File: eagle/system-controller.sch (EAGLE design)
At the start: 226 parts, among them J1 1, Q1 MOSFET-P-N-PAIR, Q10 MOSFET-P-N-PAIR, Q11 DNP/NTR4101P, Q2 MOSFET-P-N-PAIR, Q3 DON3035L, Q4 MOSFET-P-N-PAIR, Q5 MOSFET-P-N-PAIR, Q6 MOSFET-P-N-PAIR, Q7 MOSFET-P-N-PAIR, Q8 MOSFET-P-N-PAIR, Q9 DNP/NTR4101P, U1 TPS25944LRVCRWQFN-20-3X4, U10 TPS25944LRVCRWQFN-20-3X4, U11 ACPL-M61L, U12 ACPL-M61L, U13 TPS25944LRVCRWQFN-20-3X4, U14 ACPL-M61L, U15 ACPL-M61L, U2 LP5907MFX-3.0, U3 TPS25944LRVCRWQFN-20-3X4, U4 TPS25944LRVCRWQFN-20-3X4, U5 TPS25944LRVCRWQFN-20-3X4, U6 TPS25944LRVCRWQFN-20-3X4, U7 ATMEGA128L-8A(U/N), U8 TS4100, U9 TPS25944LRVCRWQFN-20-3X4, X1 8 MHz CRYSTAL-ABRACON-ABM3-SMD

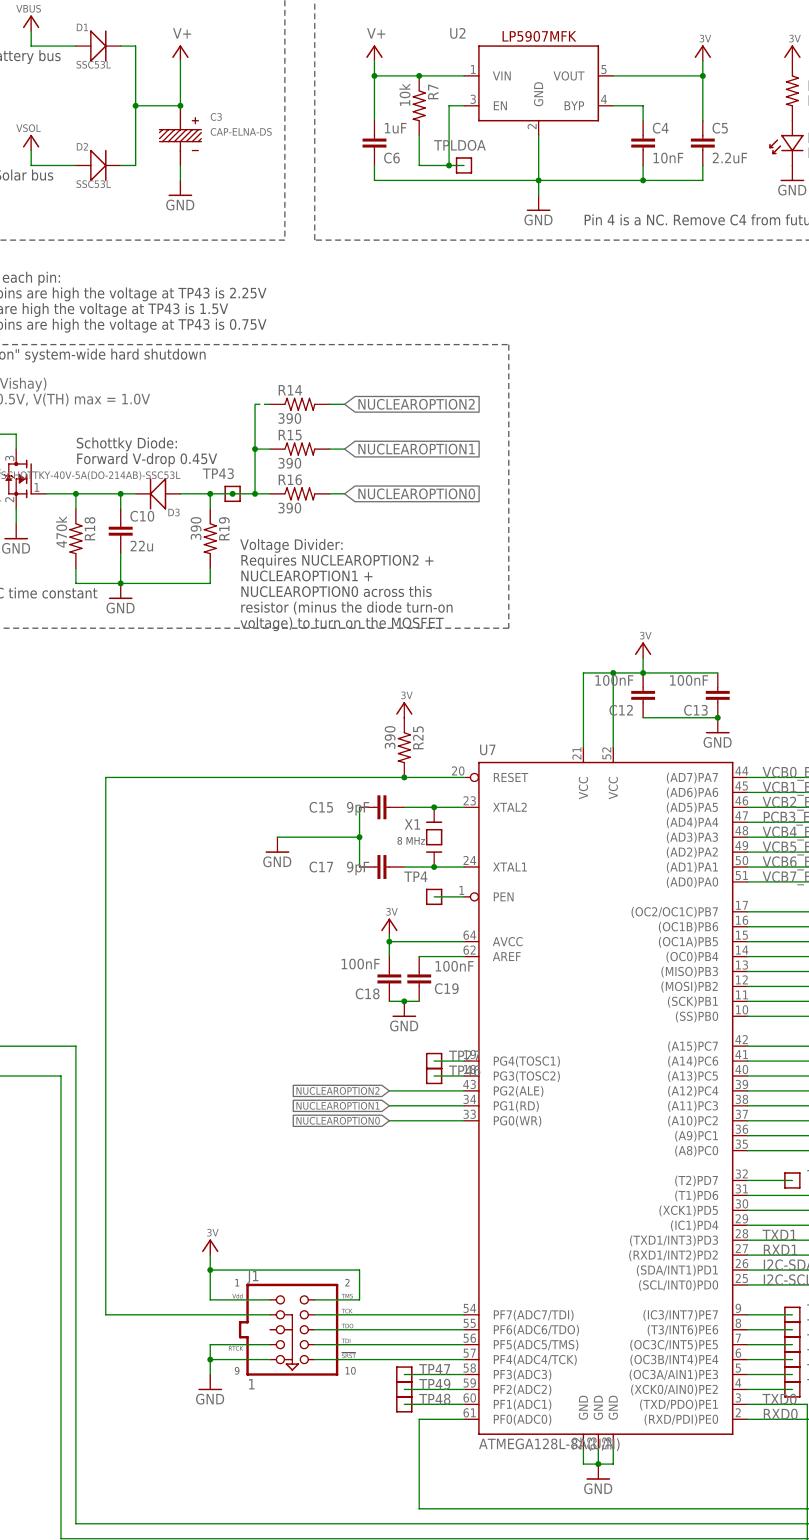
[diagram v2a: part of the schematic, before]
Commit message: Fixed some of the remaining issues such as JTAG layout and schematic, 0 ohm resistors, etc. Check the issue section on the git for more info
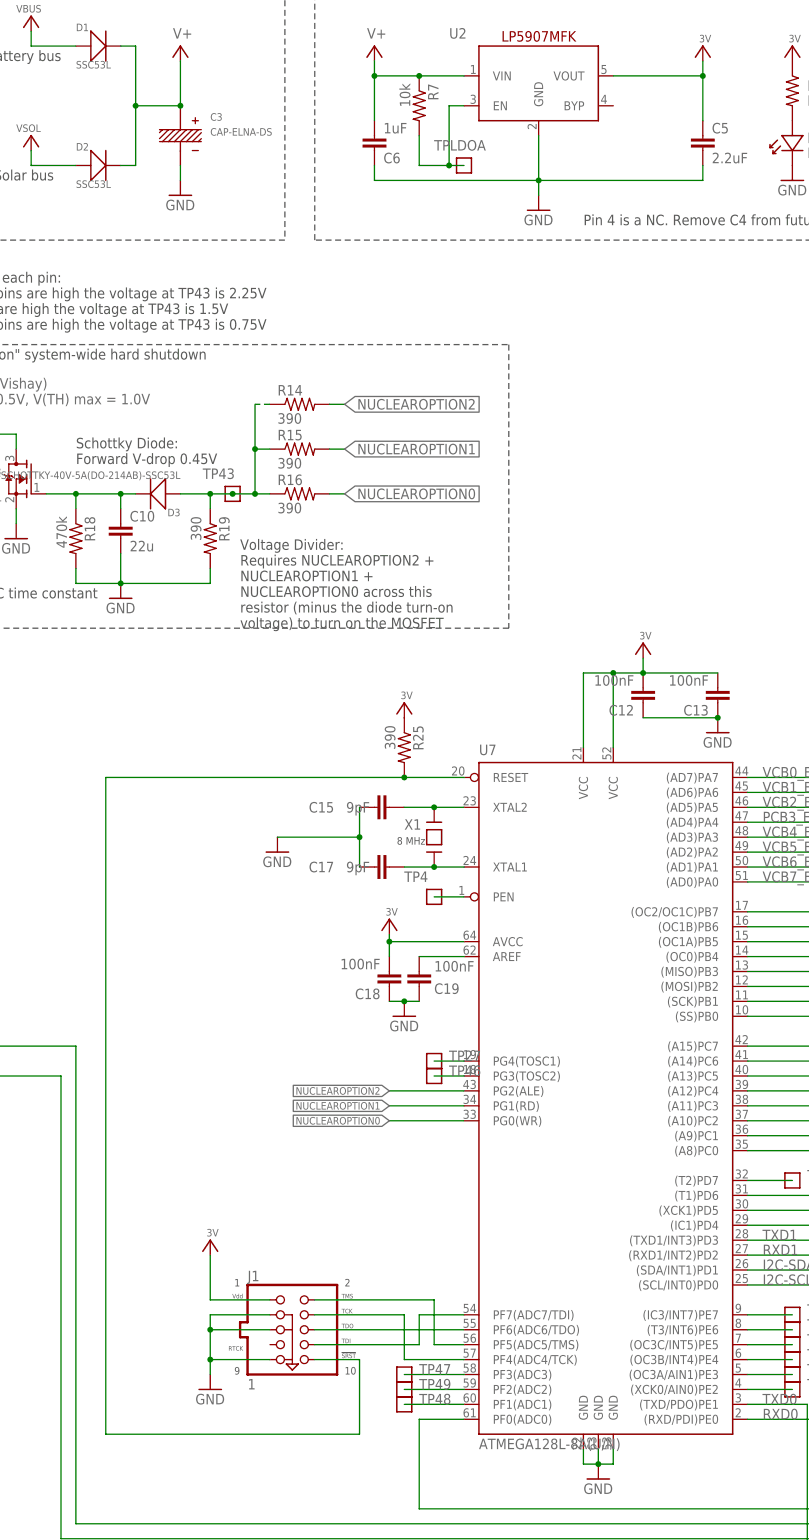
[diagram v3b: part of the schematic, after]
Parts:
- removed C4: 10nF, rcl_custom:C-EU0603-B-NOSILK
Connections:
- removed net N$23: C4.1, U2.BYP
- net 3V: no longer J1.TMS
- net GND: now also J1.GND3, J1.GND5; no longer C4.2, J1.RTCK
- net N$11: now also J1.TCK; no longer J1.SRST
- net N$13: now also U7.PF7(ADC7/TDI); no longer U7.PF5(ADC5/TMS)
- net N$14: now also J1.TMS, U7.PF5(ADC5/TMS); no longer J1.TCK, U7.PF7(ADC7/TDI)
- net N$15: now also J1.SRST; no longer J1.GND3
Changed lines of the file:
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@@
 <?xml version="1.0" encoding="utf-8"?>
 <!DOCTYPE eagle SYSTEM "eagle.dtd">
-<eagle version="7.5.0">
+<eagle version="7.6.0">
 <drawing>
 <settings>
@@
 <attribute name="MPN" value="CL10A225KQ8NNNC"/>
 </part>
-<part name="C4" library="rcl_custom" deviceset="C-EU" device="0603-B-NOSILK" value="10nF">
-<attribute name="DIST" value="digikey"/>
-<attribute name="DPN" value="399-1092-1-ND"/>
-<attribute name="MFN" value="Kemet"/>
-<attribute name="MPN" value="C0603C103J5RACTU"/>
-</part>
 <part name="SUPPLY9" library="psas_c3_team05" deviceset="V+" device=""/>
 <part name="X1" library="crystal-abracon-abm3-smd" deviceset="CRYSTAL-ABRACON-ABM3-SMD" device="" value="8 MHz CRYSTAL-ABRACON-ABM3-SMD">
@@
 <attribute name="MPN" x="195.58" y="378.46" size="1.778" layer="96" display="off"/>
 </instance>
-<instance part="C4" gate="CE" x="185.42" y="378.46">
-<attribute name="DIST" x="185.42" y="378.46" size="1.778" layer="96" display="off"/>
-<attribute name="DPN" x="185.42" y="378.46" size="1.778" layer="96" display="off"/>
-<attribute name="MFN" x="185.42" y="378.46" size="1.778" layer="96" display="off"/>
-<attribute name="MPN" x="185.42" y="378.46" size="1.778" layer="96" display="off"/>
-</instance>
 <instance part="SUPPLY9" gate="1" x="106.68" y="393.7"/>
 <instance part="X1" gate="G$1" x="149.86" y="259.08" smashed="yes" rot="R270">
@@
 </segment>
 </net>
-<net name="N$11" class="0">
-<segment>
-<pinref part="U7" gate="G$1" pin="PF4(ADC4/TCK)"/>
-<wire x1="129.54" y1="170.18" x2="154.94" y2="170.18" width="0.1524" layer="91"/>
-<pinref part="J1" gate="J" pin="SRST"/>
-</segment>
-</net>
-<net name="N$12" class="0">
-<segment>
-<pinref part="U7" gate="G$1" pin="PF6(ADC6/TDO)"/>
-<wire x1="129.54" y1="175.26" x2="154.94" y2="175.26" width="0.1524" layer="91"/>
-<pinref part="J1" gate="J" pin="TDO"/>
-</segment>
-</net>
-<net name="N$13" class="0">
-<segment>
-<pinref part="U7" gate="G$1" pin="PF5(ADC5/TMS)"/>
-<wire x1="129.54" y1="172.72" x2="154.94" y2="172.72" width="0.1524" layer="91"/>
-<pinref part="J1" gate="J" pin="TDI"/>
-</segment>
-</net>
-<net name="N$14" class="0">
-<segment>
-<pinref part="U7" gate="G$1" pin="PF7(ADC7/TDI)"/>
-<wire x1="129.54" y1="177.8" x2="154.94" y2="177.8" width="0.1524" layer="91"/>
-<pinref part="J1" gate="J" pin="TCK"/>
-</segment>
-</net>
 <net name="N$15" class="0">
 <segment>
@@
 <wire x1="154.94" y1="269.24" x2="144.78" y2="269.24" width="0.1524" layer="91"/>
 <wire x1="144.78" y1="269.24" x2="93.98" y2="269.24" width="0.1524" layer="91"/>
-<wire x1="93.98" y1="269.24" x2="93.98" y2="177.8" width="0.1524" layer="91"/>
-<wire x1="93.98" y1="177.8" x2="121.92" y2="177.8" width="0.1524" layer="91"/>
+<wire x1="93.98" y1="269.24" x2="93.98" y2="157.48" width="0.1524" layer="91"/>
 <pinref part="R25" gate="R" pin="2"/>
 <junction x="144.78" y="269.24"/>
-<pinref part="J1" gate="J" pin="GND3"/>
+<wire x1="93.98" y1="157.48" x2="137.16" y2="157.48" width="0.1524" layer="91"/>
+<wire x1="137.16" y1="157.48" x2="137.16" y2="170.18" width="0.1524" layer="91"/>
+<pinref part="J1" gate="J" pin="SRST"/>
+<wire x1="137.16" y1="170.18" x2="129.54" y2="170.18" width="0.1524" layer="91"/>
 </segment>
 </net>
@@
 </segment>
 </net>
-<net name="N$23" class="0">
-<segment>
-<pinref part="C4" gate="CE" pin="1"/>
-<wire x1="180.34" y1="383.54" x2="185.42" y2="383.54" width="0.1524" layer="91"/>
-<wire x1="185.42" y1="383.54" x2="185.42" y2="381" width="0.1524" layer="91"/>
-<pinref part="U2" gate="G$1" pin="BYP"/>
-</segment>
-</net>
 <net name="N$1" class="0">
 <segment>
@@
 </segment>
 <segment>
-<wire x1="137.16" y1="185.42" x2="137.16" y2="180.34" width="0.1524" layer="91"/>
-<wire x1="111.76" y1="185.42" x2="137.16" y2="185.42" width="0.1524" layer="91"/>
 <wire x1="121.92" y1="180.34" x2="111.76" y2="180.34" width="0.1524" layer="91"/>
-<wire x1="111.76" y1="180.34" x2="111.76" y2="185.42" width="0.1524" layer="91"/>
+<wire x1="111.76" y1="180.34" x2="111.76" y2="187.96" width="0.1524" layer="91"/>
 <pinref part="3V-3" gate="G$1" pin="3V"/>
-<wire x1="111.76" y1="187.96" x2="111.76" y2="185.42" width="0.1524" layer="91"/>
-<junction x="111.76" y="185.42"/>
 <pinref part="J1" gate="J" pin="VDD"/>
-<pinref part="J1" gate="J" pin="TMS"/>
-<wire x1="129.54" y1="180.34" x2="137.16" y2="180.34" width="0.1524" layer="91"/>
 </segment>
 <segment>
@@
 <pinref part="C5" gate="CE" pin="2"/>
 <wire x1="195.58" y1="370.84" x2="195.58" y2="373.38" width="0.1524" layer="91"/>
-<wire x1="167.64" y1="370.84" x2="185.42" y2="370.84" width="0.1524" layer="91"/>
-<pinref part="C4" gate="CE" pin="2"/>
-<wire x1="185.42" y1="370.84" x2="195.58" y2="370.84" width="0.1524" layer="91"/>
-<wire x1="185.42" y1="373.38" x2="185.42" y2="370.84" width="0.1524" layer="91"/>
-<junction x="185.42" y="370.84"/>
+<wire x1="167.64" y1="370.84" x2="195.58" y2="370.84" width="0.1524" layer="91"/>
 <pinref part="C6" gate="CE" pin="1"/>
 <pinref part="U2" gate="G$1" pin="GND"/>
@@
 <segment>
 <pinref part="GND3" gate="1" pin="GND"/>
-<wire x1="121.92" y1="172.72" x2="111.76" y2="172.72" width="0.1524" layer="91"/>
-<wire x1="111.76" y1="172.72" x2="111.76" y2="170.18" width="0.1524" layer="91"/>
 <wire x1="121.92" y1="170.18" x2="111.76" y2="170.18" width="0.1524" layer="91"/>
 <junction x="111.76" y="170.18"/>
 <wire x1="111.76" y1="170.18" x2="111.76" y2="167.64" width="0.1524" layer="91"/>
 <pinref part="J1" gate="J" pin="GND9"/>
-<pinref part="J1" gate="J" pin="RTCK"/>
+<pinref part="J1" gate="J" pin="GND5"/>
+<wire x1="121.92" y1="175.26" x2="111.76" y2="175.26" width="0.1524" layer="91"/>
+<wire x1="111.76" y1="175.26" x2="111.76" y2="170.18" width="0.1524" layer="91"/>
+<pinref part="J1" gate="J" pin="GND3"/>
+<wire x1="121.92" y1="177.8" x2="111.76" y2="177.8" width="0.1524" layer="91"/>
+<wire x1="111.76" y1="177.8" x2="111.76" y2="175.26" width="0.1524" layer="91"/>
+<junction x="111.76" y="175.26"/>
 </segment>
 <segment>
@@
 </segment>
 </net>
+<net name="N$11" class="0">
+<segment>
+<pinref part="J1" gate="J" pin="TCK"/>
+<wire x1="129.54" y1="177.8" x2="144.78" y2="177.8" width="0.1524" layer="91"/>
+<wire x1="144.78" y1="177.8" x2="144.78" y2="170.18" width="0.1524" layer="91"/>
+<pinref part="U7" gate="G$1" pin="PF4(ADC4/TCK)"/>
+<wire x1="144.78" y1="170.18" x2="154.94" y2="170.18" width="0.1524" layer="91"/>
+</segment>
+</net>
+<net name="N$12" class="0">
+<segment>
+<pinref part="J1" gate="J" pin="TDO"/>
+<pinref part="U7" gate="G$1" pin="PF6(ADC6/TDO)"/>
+<wire x1="129.54" y1="175.26" x2="154.94" y2="175.26" width="0.1524" layer="91"/>
+</segment>
+</net>
+<net name="N$13" class="0">
+<segment>
+<pinref part="J1" gate="J" pin="TDI"/>
+<wire x1="129.54" y1="172.72" x2="147.32" y2="172.72" width="0.1524" layer="91"/>
+<wire x1="147.32" y1="172.72" x2="147.32" y2="177.8" width="0.1524" layer="91"/>
+<pinref part="U7" gate="G$1" pin="PF7(ADC7/TDI)"/>
+<wire x1="147.32" y1="177.8" x2="154.94" y2="177.8" width="0.1524" layer="91"/>
+</segment>
+</net>
+<net name="N$14" class="0">
+<segment>
+<pinref part="J1" gate="J" pin="TMS"/>
+<wire x1="129.54" y1="180.34" x2="149.86" y2="180.34" width="0.1524" layer="91"/>
+<wire x1="149.86" y1="180.34" x2="149.86" y2="172.72" width="0.1524" layer="91"/>
+<pinref part="U7" gate="G$1" pin="PF5(ADC5/TMS)"/>
+<wire x1="149.86" y1="172.72" x2="154.94" y2="172.72" width="0.1524" layer="91"/>
+</segment>
+</net>

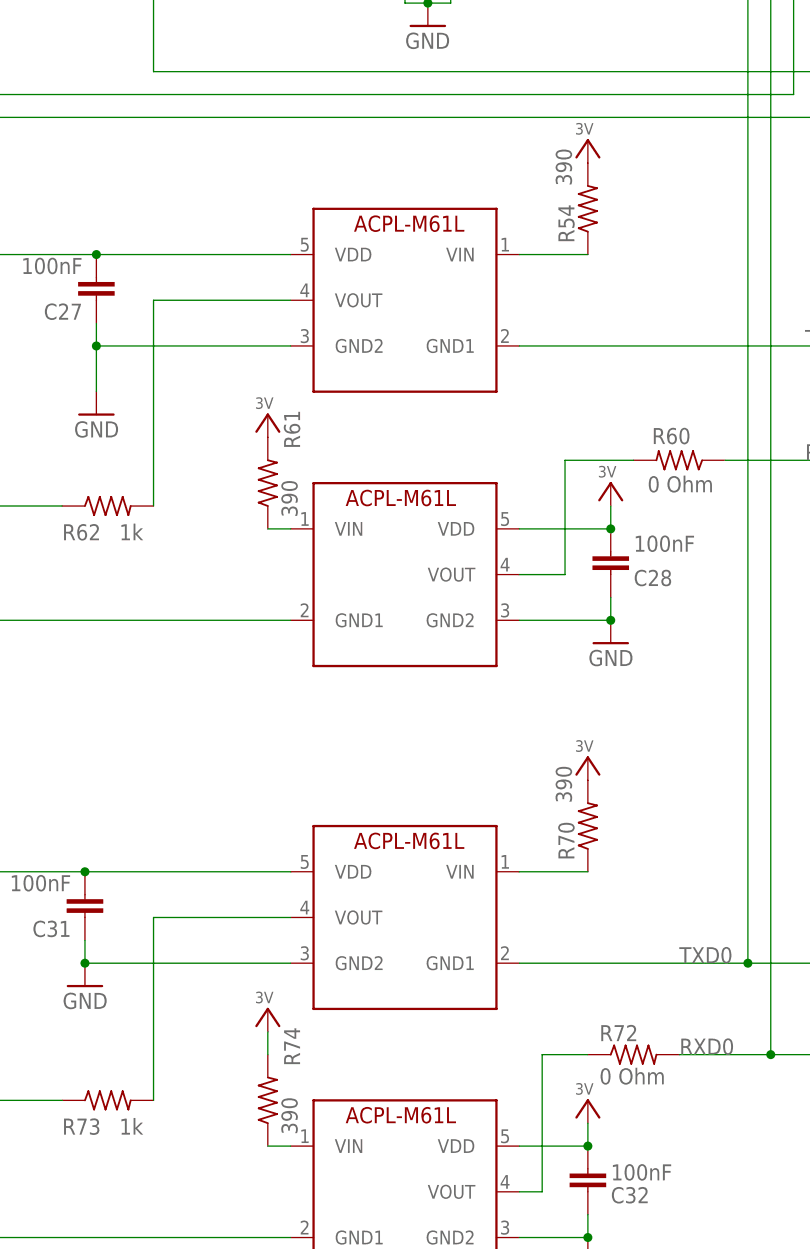
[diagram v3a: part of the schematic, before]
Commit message: fixed reference designator and origin on optoisolator
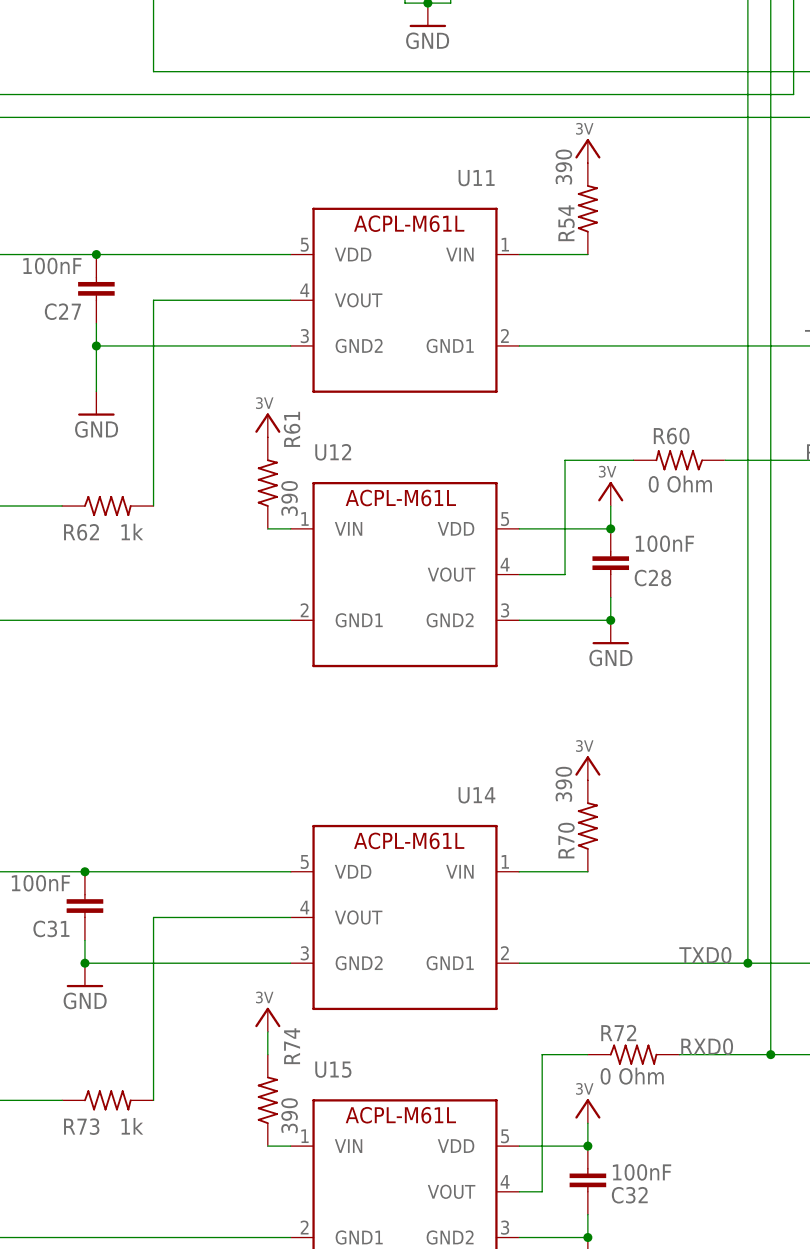
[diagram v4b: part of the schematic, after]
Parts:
- U11, U12, U14, U15: device system-controller:ACPL-M61L -> v2_sync_box:ACPL-M61L
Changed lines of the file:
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@@
 <?xml version="1.0" encoding="utf-8"?>
 <!DOCTYPE eagle SYSTEM "eagle.dtd">
-<eagle version="7.6.0">
+<eagle version="7.3.0">
 <drawing>
 <settings>
@@
 <layer number="56" name="wert" color="7" fill="1" visible="no" active="no"/>
 <layer number="57" name="tCAD" color="7" fill="1" visible="no" active="no"/>
+<layer number="58" name="b3D" color="7" fill="1" visible="no" active="no"/>
 <layer number="59" name="Invisible" color="7" fill="1" visible="no" active="no"/>
 <layer number="61" name="stand" color="7" fill="1" visible="no" active="no"/>
@@
 <layer number="112" name="tSilk" color="7" fill="1" visible="no" active="yes"/>
 <layer number="113" name="ReferenceLS" color="7" fill="1" visible="no" active="yes"/>
+<layer number="114" name="secv1" color="7" fill="1" visible="yes" active="yes"/>
+<layer number="115" name="secv12" color="7" fill="1" visible="yes" active="yes"/>
 <layer number="116" name="Patch_BOT" color="7" fill="1" visible="no" active="yes"/>
+<layer number="117" name="secv21" color="7" fill="1" visible="yes" active="yes"/>
 <layer number="118" name="Rect_Pads" color="7" fill="1" visible="no" active="yes"/>
 <layer number="121" name="_tsilk" color="7" fill="1" visible="no" active="yes"/>
@@
 <layer number="127" name="_tValues" color="7" fill="1" visible="no" active="yes"/>
 <layer number="128" name="_bValues" color="7" fill="1" visible="no" active="yes"/>
+<layer number="130" name="bLogo" color="7" fill="1" visible="yes" active="yes"/>
 <layer number="131" name="tAdjust" color="7" fill="1" visible="no" active="yes"/>
 <layer number="132" name="bAdjust" color="7" fill="1" visible="no" active="yes"/>
@@
 <layer number="223" name="223bmp" color="7" fill="1" visible="no" active="yes"/>
 <layer number="224" name="224bmp" color="7" fill="1" visible="no" active="yes"/>
+<layer number="225" name="225bmp" color="7" fill="1" visible="yes" active="yes"/>
+<layer number="226" name="226bmp" color="7" fill="1" visible="yes" active="yes"/>
+<layer number="227" name="227bmp" color="7" fill="1" visible="yes" active="yes"/>
+<layer number="228" name="228bmp" color="7" fill="1" visible="yes" active="yes"/>
 <layer number="231" name="Eagle3D_PG1" color="7" fill="1" visible="no" active="yes"/>
 <layer number="232" name="Eagle3D_PG2" color="7" fill="1" visible="no" active="yes"/>
@@
 <attribute name="MPN" value="LP5907MFX-3.0/NOPB"/>
 </part>
-<part name="U11" library="system-controller" deviceset="ACPL-M61L" device="">
+<part name="U11" library="v2_sync_box" deviceset="ACPL-M61L" device="">
 <attribute name="DIST" value="digikey"/>
 <attribute name="DPN" value="516-2169-5-ND"/>
@@
 <attribute name="MPN" value="ACPL-M61L-000E"/>
 </part>
-<part name="U12" library="system-controller" deviceset="ACPL-M61L" device="">
+<part name="U12" library="v2_sync_box" deviceset="ACPL-M61L" device="">
 <attribute name="DIST" value="digikey"/>
 <attribute name="DPN" value="516-2169-5-ND"/>
@@
 <attribute name="MPN" value="ACPL-M61L-000E"/>
 </part>
-<part name="U14" library="system-controller" deviceset="ACPL-M61L" device="">
+<part name="U14" library="v2_sync_box" deviceset="ACPL-M61L" device="">
 <attribute name="DIST" value="digikey"/>
 <attribute name="DPN" value="516-2169-5-ND"/>
@@
 <attribute name="MPN" value="ACPL-M61L-000E"/>
 </part>
-<part name="U15" library="system-controller" deviceset="ACPL-M61L" device="">
+<part name="U15" library="v2_sync_box" deviceset="ACPL-M61L" device="">
 <attribute name="DIST" value="digikey"/>
 <attribute name="DPN" value="516-2169-5-ND"/>
